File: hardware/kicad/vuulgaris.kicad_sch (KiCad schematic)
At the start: 308 parts, among them J1 TFPUSH, J10 PJ-603_C41409498, J11 TYPE-C-31-M-12, J12 FACEPLATE 2x5 IDC, J2 PJ-376, J3 PJ-376, J4 PJ-376, J5 PJ-376, J6 PJ-376, J7 PJ-603_C41409498, J8 PJ-603_C41409498, J9 PJ-603_C41409498, Q1 J113 / MMBFJ113, Q2 J113 / MMBFJ113, SW1 SW_DPDT_FLAT, SW2 SW_DPDT_FLAT, SW4 12x12 tactile, SW5 12x12 tactile, SW6 12x12 tactile, SW7 12x12 tactile, SW8 12x12 tactile, SW9 12x12 tactile, U1 ES_DAISY_PATCH_SM_REV1, U10 OPA1688_FLAT, U101 V3205SD, U102 TL072_FLAT, U103 TL072_FLAT, U104 CD4046B, U106 TL072_FLAT, U201 V3205SD, U202 TL072_FLAT, U203 TL072_FLAT, U204 CD4046B, U206 TL072_FLAT, U3 MCP23017-E_SO, U301 TL084, U302 TL074, U4 MCP23017-E_SO, U401 TL084, U402 TL074, U5 AMS1117-3.3, U6 AMS1117-3.3, U7 DKM10E-12, U8 78L05, U9 OPA1688_FLAT

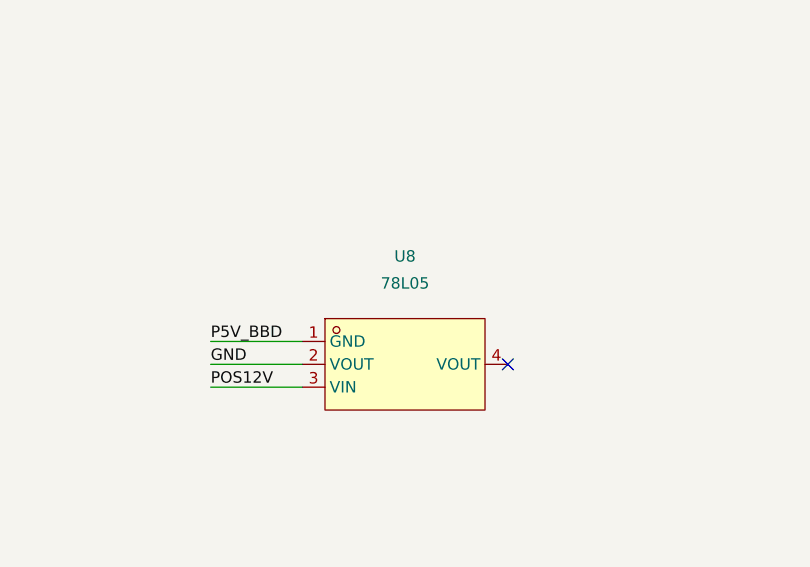
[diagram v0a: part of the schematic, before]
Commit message: hardware: U8 was still labelled 78L05 after being changed to AMS1117-5.0
Building the BOM surfaced it. U8 carries the value 78L05 but sits in a SOT-223
footprint, and power-usbc-dkm.md:140 records the change: "U8: 78L05 (SOT-89) ->
AMS1117-5.0 (SOT-223), 2026-09-07". The footprint was swapped, the value string
was not.

Ordered as written that buys a 78L05 that does not fit the pads -- and if
anyone forced it in, the part deliberately designed out for having no defensible
thermal margin on this rail.

The netlist was already correct: U8.3 POS12V in, U8.1 P5V_BBD out, U8.2 GND, which
is AMS1117 SOT-223 pin order rather than 78L05's. Only the label was wrong, and
only the BOM would ever have shown it.

939/939 connections verified after regenerating.
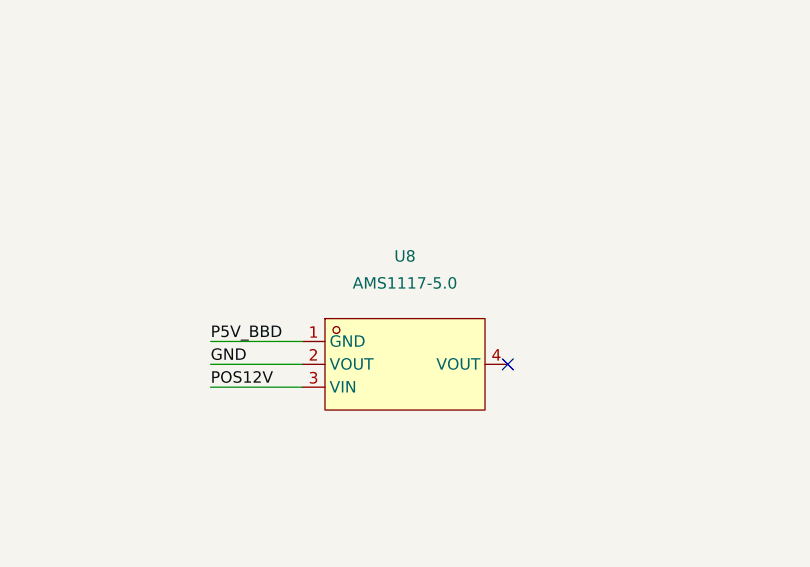
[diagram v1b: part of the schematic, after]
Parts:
- U8: value 78L05 -> AMS1117-5.0
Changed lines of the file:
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@@
     (in_bom yes) (on_board yes) (dnp no)
     (property "Reference" "U8" (at 420 2388 0) (effects (font (size 1.27 1.27))))
-    (property "Value" "78L05" (at 420 2391 0) (effects (font (size 1.27 1.27))))
+    (property "Value" "AMS1117-5.0" (at 420 2391 0) (effects (font (size 1.27 1.27))))
     (property "Footprint" "vuulgaris:SOT-223-3_L6.5-W3.4-P2.30-LS7.0-BR" (at 420 2400 0) (effects (font (size 1.27 1.27)) hide))
     (property "Datasheet" "" (at 420 2400 0) (effects (font (size 1.27 1.27)) hide))

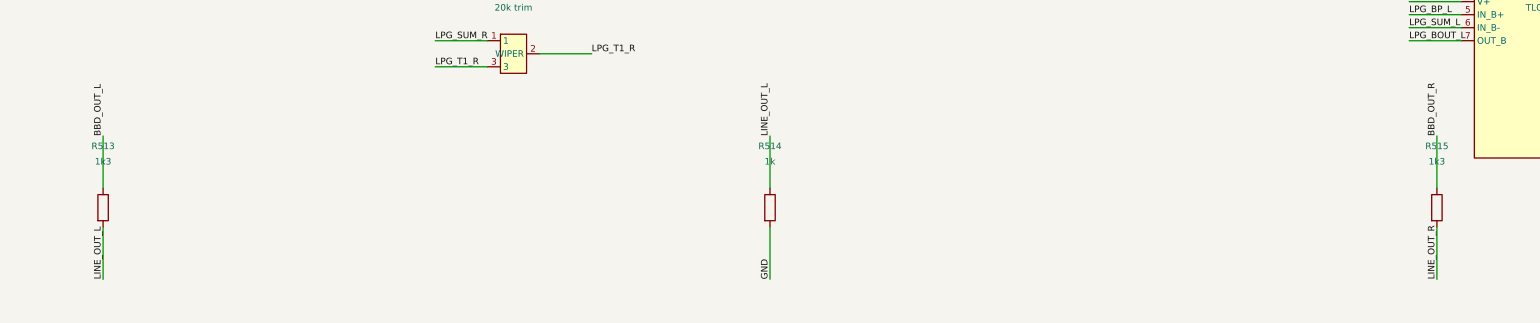
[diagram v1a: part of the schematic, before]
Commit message: hardware: BOM built out -- 69 of 79 lines sourced, Basic parts where they exist
mkbom.py resolves LCSC numbers from four sources in order of confidence: a
curated table of decisions verified against LCSC or JLCPCB product pages, codes
embedded in a footprint or value name, the designator tables in docs/, and
JLCPCB's Basic parts list matched on value, package and dielectric.

Basic matters because JLC charges a per-part loading fee for every distinct
Extended part. 26 lines land on Basic parts, covering roughly 180 of the 293
components -- every common resistor value, 100nF, 1uF 50V, 10uF, the 0402s.

Two things fell out of the sourcing rather than the design.

R513/R515 were 1k3, which is not a Basic part. 1k2 is, with 101,727 in stock,
and it is also closer to the target: the line output goes from +3.89dBu to
+4.21dBu against a +4dBu aim. Changed, 939/939 connections still verified.

U8's value was 78L05 while its footprint was SOT-223 -- the part was changed to
AMS1117-5.0 on 2026-09-07 and the label never followed. Ordered as written that
buys a part that does not fit the pads. Caught only because the BOM makes every
value legible in one place.

Ten lines remain. Four are the known hand-solder set with no LCSC source at all:
V3205SD, VTL5C3, the DW3 switches and the Daisy module. Six want a real lookup:
4R7 0603, 3.3uF 0805, the ferrite bead, and three C0G values (2nF, 4.7nF, 15nF)
that are not in the Basic list and should stay C0G, since they set filter
corners in the LPG and BBD paths where an X7R would drift with temperature and
signal level.
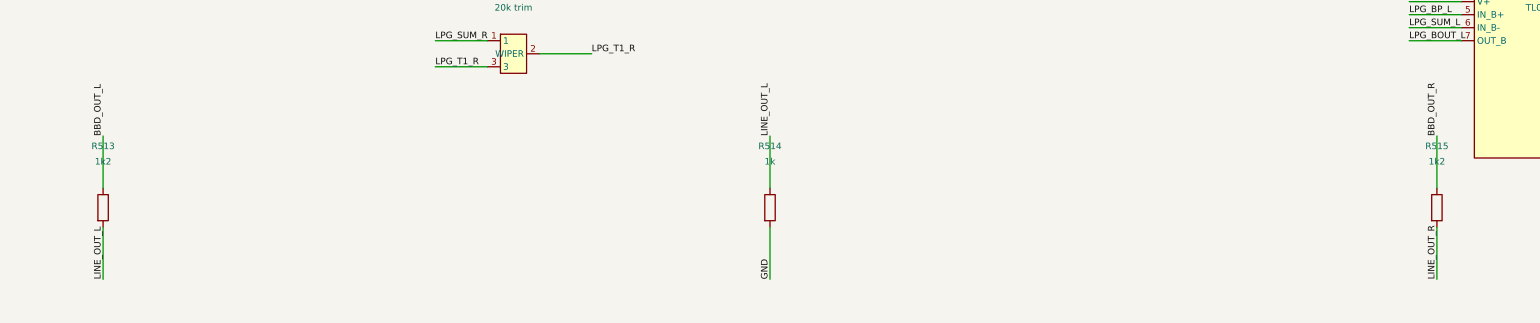
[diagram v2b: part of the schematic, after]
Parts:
- R513, R515: value 1k3 -> 1k2
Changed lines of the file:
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@@
     (in_bom yes) (on_board yes) (dnp no)
     (property "Reference" "R513" (at 640 3918 0) (effects (font (size 1.27 1.27))))
-    (property "Value" "1k3" (at 640 3921 0) (effects (font (size 1.27 1.27))))
+    (property "Value" "1k2" (at 640 3921 0) (effects (font (size 1.27 1.27))))
     (property "Footprint" "vuulgaris:R0603" (at 640 3930 0) (effects (font (size 1.27 1.27)) hide))
     (property "Datasheet" "" (at 640 3930 0) (effects (font (size 1.27 1.27)) hide))
@@
     (in_bom yes) (on_board yes) (dnp no)
     (property "Reference" "R515" (at 900 3918 0) (effects (font (size 1.27 1.27))))
-    (property "Value" "1k3" (at 900 3921 0) (effects (font (size 1.27 1.27))))
+    (property "Value" "1k2" (at 900 3921 0) (effects (font (size 1.27 1.27))))
     (property "Footprint" "vuulgaris:R0603" (at 900 3930 0) (effects (font (size 1.27 1.27)) hide))
     (property "Datasheet" "" (at 900 3930 0) (effects (font (size 1.27 1.27)) hide))

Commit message: hardware: resolve the last BOM values -- one substitution, four stay Extended
Checked each of the five against JLC's Basic list and against what the part
actually does, rather than substituting on price.

C110/C210 3.3uF -> 10uF. They decouple BBD_VGG, the V3205's gate bias, 4.65V off
a 4.7k/62k divider from +5V. It is a DC bias node, so more capacitance is
strictly better; settling goes from 14ms to 44ms and nothing cares. 10uF 0805
X5R 25V is C15850, which the BOM already orders for C20/C22/C24/C25, so this
removes a line rather than adding one. 78 lines now, down from 79.

The other four stay Extended, deliberately. JLC's per-part fee is a few dollars
each and every one of them is somewhere the value or the dielectric matters:

  4R7           Basic has nothing under 10ohm but 0R. This sets U9's output
                impedance; 0R would work electrically but loses the isolation
                from cable capacitance.
  2nF C0G       2nF is not an E12 value. 2.2nF with R4's 470k moves the CV time
                constant from 940us to 1.03ms, which is inaudible.
  4.7nF C0G     sets the VCF corner. An X7R would move it with temperature and
                signal level.
  15nF C0G      this is the BBD sample-and-hold cap. X7R dielectric absorption
                would show up as droop between samples.

Each carries that reasoning in the BOM's Note column, so whoever fills them in
at order time knows what is and is not an acceptable substitution.
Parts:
- C110, C210: value 3.3uF -> 10uF
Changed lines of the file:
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@@
     (in_bom yes) (on_board yes) (dnp no)
     (property "Reference" "C110" (at 870 988 0) (effects (font (size 1.27 1.27))))
-    (property "Value" "3.3uF" (at 870 991 0) (effects (font (size 1.27 1.27))))
+    (property "Value" "10uF" (at 870 991 0) (effects (font (size 1.27 1.27))))
     (property "Footprint" "vuulgaris:C0805" (at 870 1000 0) (effects (font (size 1.27 1.27)) hide))
     (property "Datasheet" "" (at 870 1000 0) (effects (font (size 1.27 1.27)) hide))
@@
     (in_bom yes) (on_board yes) (dnp no)
     (property "Reference" "C210" (at 870 1688 0) (effects (font (size 1.27 1.27))))
-    (property "Value" "3.3uF" (at 870 1691 0) (effects (font (size 1.27 1.27))))
+    (property "Value" "10uF" (at 870 1691 0) (effects (font (size 1.27 1.27))))
     (property "Footprint" "vuulgaris:C0805" (at 870 1700 0) (effects (font (size 1.27 1.27)) hide))
     (property "Datasheet" "" (at 870 1700 0) (effects (font (size 1.27 1.27)) hide))

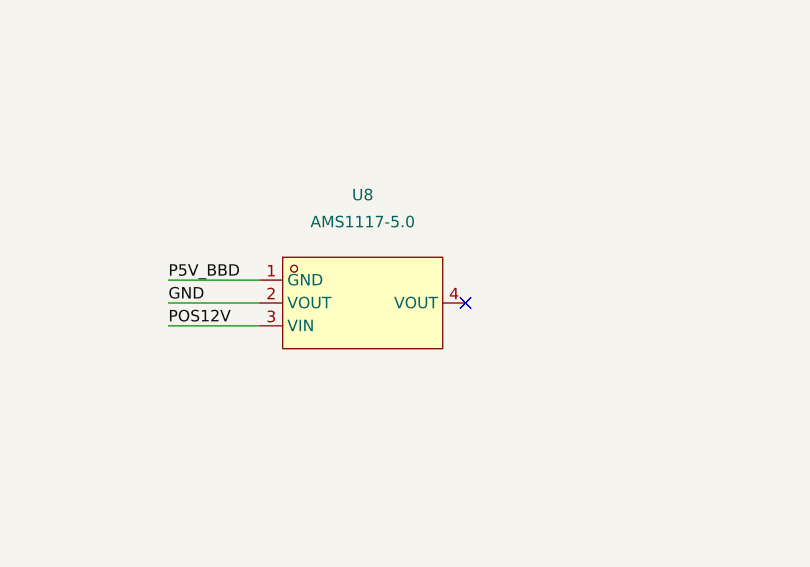
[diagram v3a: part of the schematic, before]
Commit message: hardware: U8 was wired to the 78L05 pinout, not the AMS1117's
U8 was changed from a 78L05 to an AMS1117-5.0 and the pin map never
followed. The AMS1117 is 1=GND, 2=VOUT, 3=VIN, tab=VOUT; the 78L05 is
1=OUT, 2=GND, 3=IN. As built the regulator's ground pin was driven by the
5V rail, its output was shorted to ground, and the tab -- also VOUT, and
the thermal path -- floated. P5V_BBD would never have come up, taking the
whole BBD core with it: U101/U201, U104/U204 and the V3205SD pair.

netcheck.py could not see it. The schematic is generated from netmap.json
and matches it exactly; both were wrong together. What caught it was
checking each pin's assigned net against the pin's NAME -- the board file
was already carrying (pinfunction "GND") on a pad sitting on /P5V_BBD.
U8 was the only such mismatch across all 308 parts, and all 14 polarised
parts check out.

Board: pads 1 and 2 swap nets, the tab joins P5V_BBD, three stubs and one
via replaced by four segments and a via at (151.187,157.995). Verified
clear by 0.2mm against every pad, trace and via, the new via lands inside
the In2.Cu plane fill, and P5V_BBD is a single island. GND island counts
are byte-identical to before the edit.

Regenerating the gerbers turned up a second defect: the previous export
had merged F.Mask into F.Silkscreen and B.Mask into B.Silkscreen -- 618
and 667 stray pad flashes in the legend layers. Every other layer matches
flash for flash. The drill file differs by exactly the one moved via.
CPL is unchanged; U8 did not move or rotate.
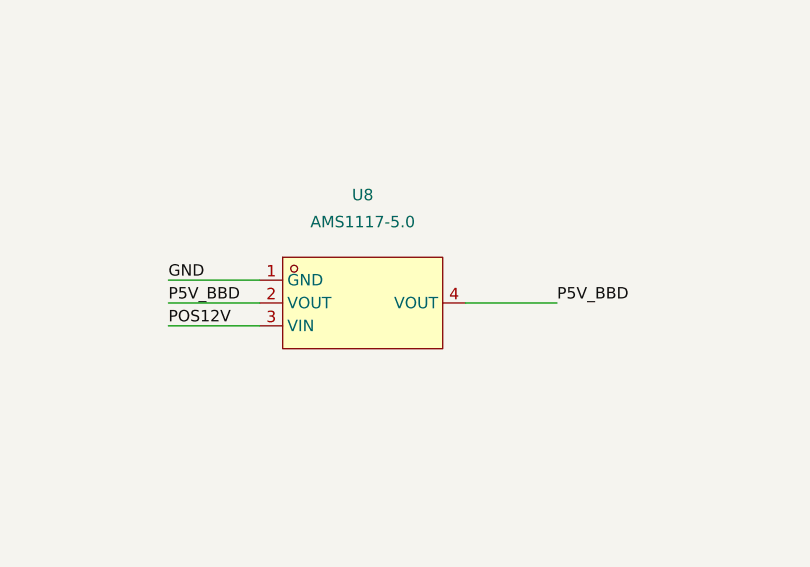
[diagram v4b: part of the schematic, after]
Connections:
- net GND: now also U8.1 (GND); no longer U8.2 (VOUT)
- net P5V_BBD: now also U8.2 (VOUT), U8.4 (VOUT); no longer U8.1 (GND)
- no-connect marks 52 -> 51
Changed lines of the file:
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@@
   (wire (pts (xy 530.0 786.03) (xy 530.0 775.87)) (stroke (width 0) (type solid)))
   (wire (pts (xy 527.46 786.03) (xy 527.46 775.87)) (stroke (width 0) (type solid)))
+  (wire (pts (xy 408.57 2397.46) (xy 398.41 2397.46)) (stroke (width 0) (type solid)))
+  (wire (pts (xy 408.57 2400.0) (xy 398.41 2400.0)) (stroke (width 0) (type solid)))
   (wire (pts (xy 408.57 2402.54) (xy 398.41 2402.54)) (stroke (width 0) (type solid)))
-  (wire (pts (xy 408.57 2400.0) (xy 398.41 2400.0)) (stroke (width 0) (type solid)))
-  (wire (pts (xy 408.57 2397.46) (xy 398.41 2397.46)) (stroke (width 0) (type solid)))
+  (wire (pts (xy 431.43 2400.0) (xy 441.59 2400.0)) (stroke (width 0) (type solid)))
   (wire (pts (xy 844.76 297.46) (xy 834.6 297.46)) (stroke (width 0) (type solid)))
   (wire (pts (xy 844.76 294.92) (xy 834.6 294.92)) (stroke (width 0) (type solid)))
@@
     (effects (font (size 1.27 1.27)) (justify left bottom))
   )
+  (label "GND" (at 398.41 2397.46 180) (fields_autoplaced)
+    (effects (font (size 1.27 1.27)) (justify left bottom))
+  )
+  (label "P5V_BBD" (at 398.41 2400.0 180) (fields_autoplaced)
+    (effects (font (size 1.27 1.27)) (justify left bottom))
+  )
   (label "POS12V" (at 398.41 2402.54 180) (fields_autoplaced)
     (effects (font (size 1.27 1.27)) (justify left bottom))
   )
-  (label "GND" (at 398.41 2400.0 180) (fields_autoplaced)
-    (effects (font (size 1.27 1.27)) (justify left bottom))
-  )
-  (label "P5V_BBD" (at 398.41 2397.46 180) (fields_autoplaced)
+  (label "P5V_BBD" (at 441.59 2400.0 0) (fields_autoplaced)
     (effects (font (size 1.27 1.27)) (justify left bottom))
   )
@@
   (no_connect (at 352.7 228.65))
   (no_connect (at 527.46 813.97))
-  (no_connect (at 431.43 2400.0))
   (sheet_instances (path "/" (page "1")))
 )

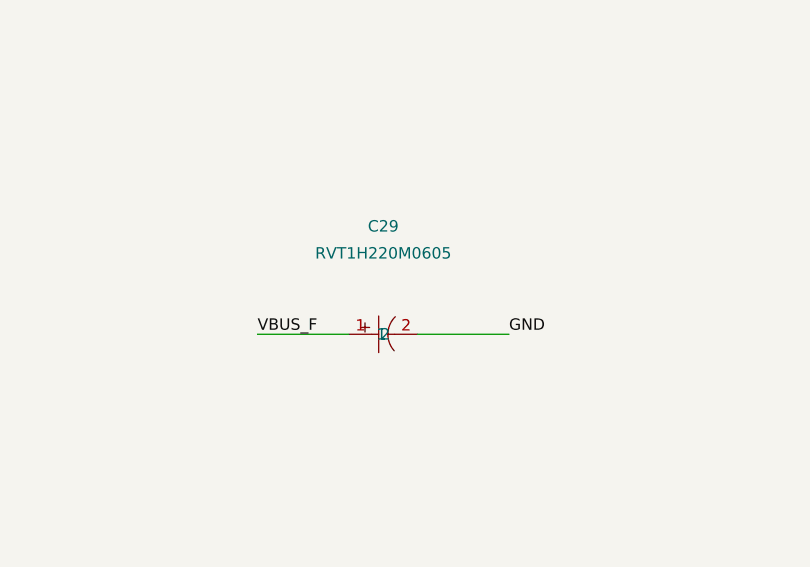
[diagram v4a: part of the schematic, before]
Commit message: hardware: add D3, an SMAJ6.0A TVS across VBUS
The source schematic carries a TVS at the USB-C connector and this board had
none: /VBUS held only C28 (10nF), F1 and the two J11 VBUS pads. F1 is a
resettable PTC, so it limits current and does nothing about voltage, and the
Mean Well spec gives the DKM10E-12 4.7-9Vdc continuous with 12Vdc tolerated for
100ms only -- the line is labelled SURGE VOLTAGE (100ms max.). A hot-plug kick
into 22uF of input bulk rings toward twice supply, which is already past
continuous spec before anything has gone wrong.

6.0A rather than the reference's 5.0A. USB VBUS is spec'd 4.75-5.25V and a 5.0V
standoff sits UNDER that ceiling, where the part leaks -- 800uA on the spec
sheet. 6.0A stands off 6.0V, clear of 5.25V, and clamps at 10.3V, inside the 12V
window. 6.5A would clamp at 11.2V, too close to it.

Placed at the connector on the back, (366.5, 66.0), in the existing cluster
beside C28: cathode to /VBUS on the 0.8mm copper already there, anode out 1.6mm
to a new GND via. A suppressor wants the shortest path to ground it can get, so
it does not move to suit the routing.

No symbol existed, so the zener graphic was cloned -- the right drawing for a
unidirectional TVS -- onto the SMA footprint already in the library. The board
footprint was generated rather than hand-typed, with the B.Cu Y-mirror and the
F->B layer mapping applied by code, and inserted as a sibling of the zone rather
than inside it, which is the mistake the U8 fix made.

Verified: 0 unconnected, 0 clearance violations, 942/942 board-schematic parity,
and D3's own CPL row reconstructs onto its real copper to 0.0000mm, cathode on
VBUS. A reversed TVS is a forward-biased short across the input, so that last
check is not optional.

No LCSC part chosen -- LCSC's search is a JS app and guessing a C-number is not
sourcing -- so it joins the BOM's unsourced list with the selection criteria in
its Note. mkbom.py now writes the JLC BOM as well as the full one; that copy had
been de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
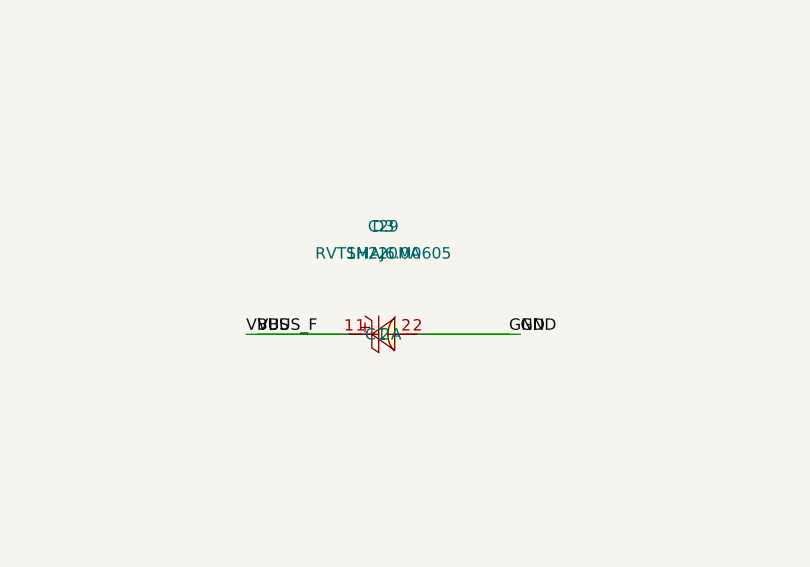
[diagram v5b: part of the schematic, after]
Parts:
- added D3: SMAJ6.0A, vuulgaris:SMA_L4.3-W2.6-LS5.2-RD, symbol vuulgaris:SMAJ6.0A
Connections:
- net VBUS_F is gone; now on net VBUS: C29.1, C30.2, C31.2, F1.2, U7.1 (+Vin)
- net GND: now also D3.2 (A)
- net VBUS: now also D3.1 (C)

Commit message: hardware: C119/C219 15nF -> 10nF C0G, the only C0G that package can hold
15nF C0G was unobtainable, not unsourced. JLC stocks no 15nF C0G/NP0 in any
SMD package, and 18nF and 22nF do not exist in 0805 either -- C0G is a low-K
dielectric and 10nF is the practical ceiling for that footprint.

The manual asks for "a relatively big capacitor" in C0G, not for 15nF exactly,
and the DIELECTRIC is the requirement: X7R dielectric absorption relaxes the
held voltage between samples and smears the reconstruction. 10nF keeps C0G.

  C237168  Walsin 0805N103J500CT, 10nF 50V NP0 5%, 149,428 in stock, $0.031

Same 0805 footprint, so no board change and nothing to hand-solder -- better
than either fallback, which were a through-hole part or cutting the pads open.

What moves: acquisition (Ron_J113 x C) gets 1.5x faster, which helps inside the
narrow sample pulse the manual describes; droop and JFET charge injection get
1.5x worse, roughly 9mV at the output after U106B's x5.55 at typical J113
off-leakage. Inside the character of a lo-fi BBD delay.

Unsourced is now 4 lines / 9 parts, all genuinely unavailable and all
through-hole: the VTL5C3 vactrols, the V3205SD pair, the DPDT switches and the
Daisy module. Separately, U7 and DS1 have LCSC numbers but JLC cannot place
them. Copper is untouched -- the value string lives on the fab layer only, and
the drill count is identical either side of this change.
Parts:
- C119, C219: value 15nF C0G 0805 -> 10nF C0G 0805
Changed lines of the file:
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@@
     (in_bom yes) (on_board yes) (dnp no)
     (property "Reference" "C119" (at 420 1068 0) (effects (font (size 1.27 1.27))))
-    (property "Value" "15nF C0G 0805" (at 420 1071 0) (effects (font (size 1.27 1.27))))
+    (property "Value" "10nF C0G 0805" (at 420 1071 0) (effects (font (size 1.27 1.27))))
     (property "Footprint" "vuulgaris:C0805" (at 420 1080 0) (effects (font (size 1.27 1.27)) hide))
     (property "Datasheet" "" (at 420 1080 0) (effects (font (size 1.27 1.27)) hide))
@@
     (in_bom yes) (on_board yes) (dnp no)
     (property "Reference" "C219" (at 420 1768 0) (effects (font (size 1.27 1.27))))
-    (property "Value" "15nF C0G 0805" (at 420 1771 0) (effects (font (size 1.27 1.27))))
+    (property "Value" "10nF C0G 0805" (at 420 1771 0) (effects (font (size 1.27 1.27))))
     (property "Footprint" "vuulgaris:C0805" (at 420 1780 0) (effects (font (size 1.27 1.27)) hide))
     (property "Datasheet" "" (at 420 1780 0) (effects (font (size 1.27 1.27)) hide))
